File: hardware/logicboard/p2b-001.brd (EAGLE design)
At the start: 91 x 90 mm, 54 parts, among them IC1 74LS06N, IC2 4066N, J1 MKR, J2 GPIO, J3 Vcc, J4 RLY, J5 SPI, J7 DIN5, J8 DIN5, J9 DIN5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

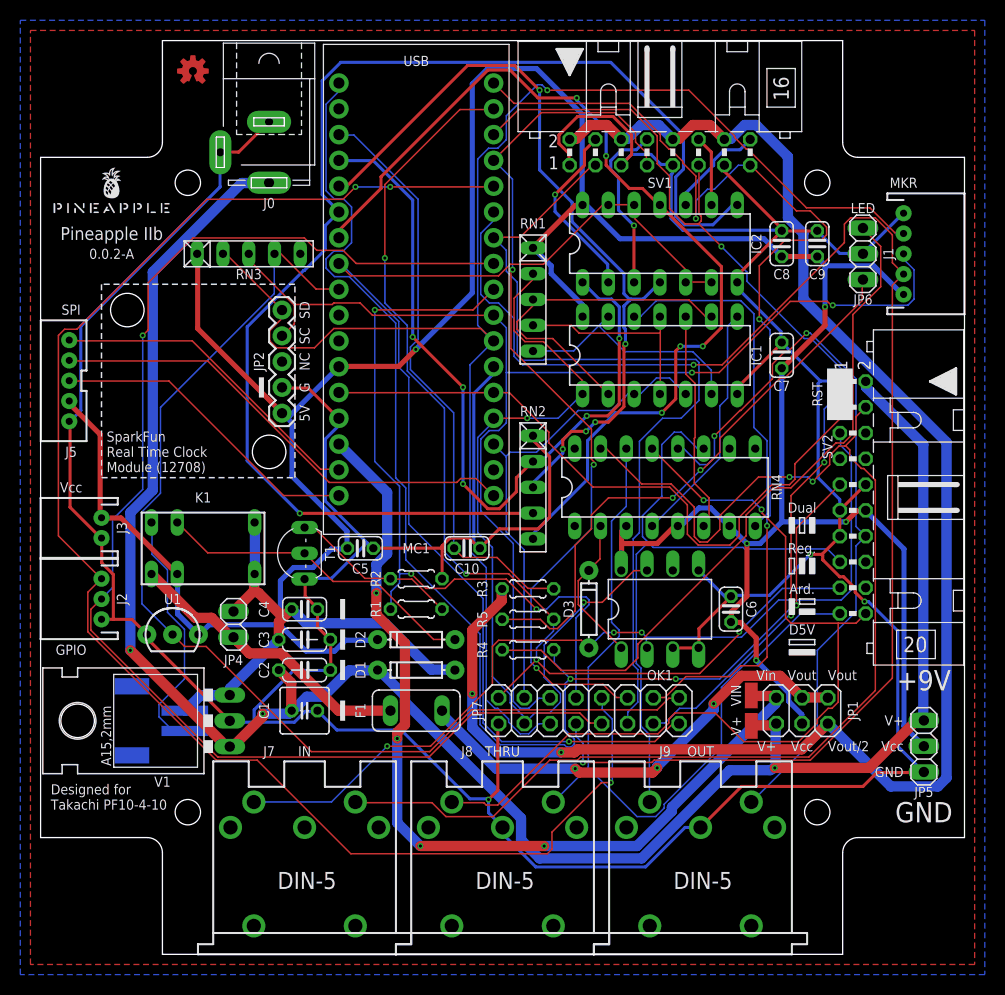
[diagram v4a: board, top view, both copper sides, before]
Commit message: Followed Pineapple II 2.4.0 design. Before autorouting.
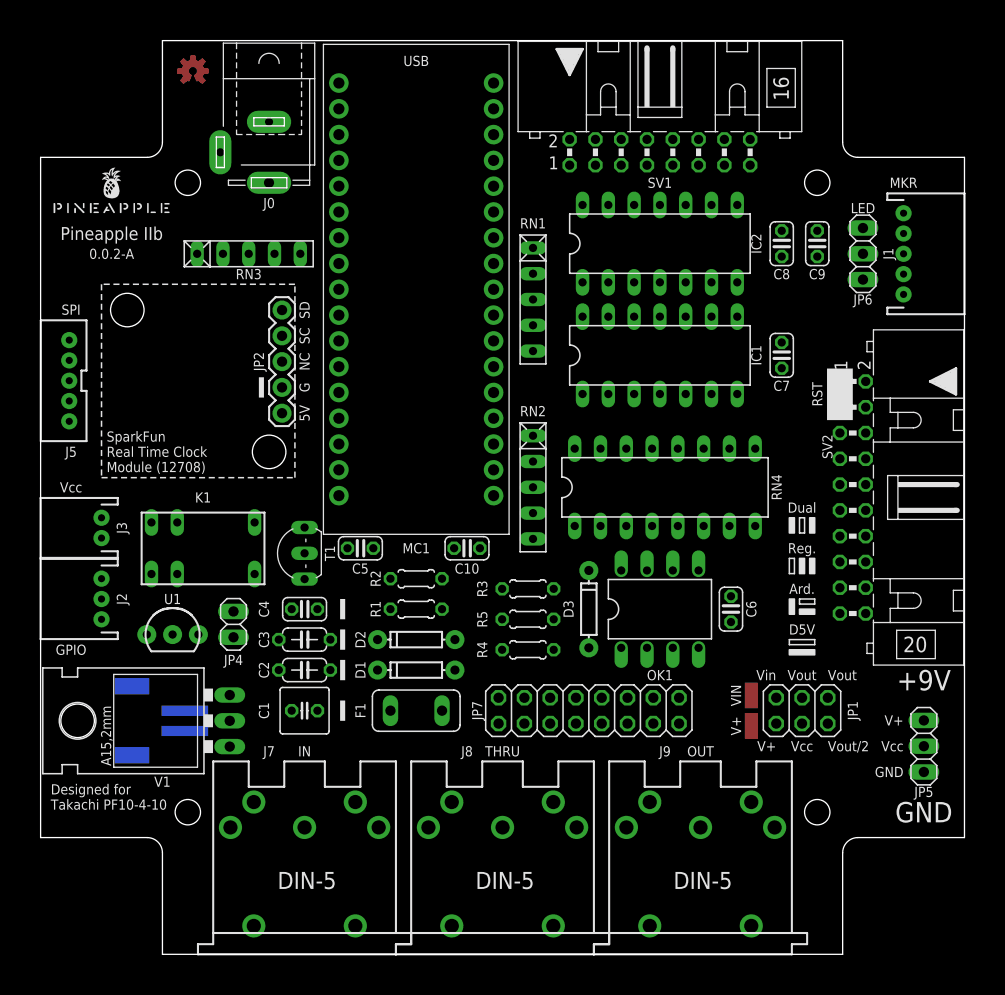
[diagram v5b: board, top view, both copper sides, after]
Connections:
- removed net D7: J1.4, JP7.7, MC1.P$6
- removed net GATE: IC2.12, IC2.13, IC2.5, IC2.6, JP7.15, MC1.P$27
- removed net LED0A: JP6.3, R4.1
- new net D7GATE: IC2.12, IC2.13, IC2.5, IC2.6, J1.4, JP7.7, MC1.P$6
- new net LED2A: JP6.1, R5.1
- new net MNTR: JP7.15, MC1.P$27, OK1.6, RN3.5
- new net MNTRA: OK1.4, RN4.16
- net GND: no longer OK1.4
- net LED1A: now also JP6.3, R4.1; no longer JP6.1, R5.1
- net VCC/2: now also RN4.1
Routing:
- net GND: track 428.7 -> 0.00 mm, vias 3 -> 0
- net VCC: track 321.2 -> 0.00 mm, vias 5 -> 0
- net V+: track 200.8 -> 0.00 mm, vias 3 -> 0
- net VCC/2: track 161.3 -> 0.00 mm, vias 2 -> 0
- net GPIO2: track 153.8 -> 0.00 mm, vias 3 -> 0
- net SDA: track 151.7 -> 0.00 mm, vias 1 -> 0
- net D7: track 144.6 -> 0.00 mm, vias 2 -> 0
- net LED1: track 133.9 -> 0.00 mm, vias 3 -> 0
- net GPIO1: track 131.2 -> 0.00 mm, vias 1 -> 0
- net ANLG3: track 127.0 -> 0.00 mm, vias 1 -> 0
- net SCL: track 124.9 -> 0.00 mm, vias 2 -> 0
- net MISND: track 122.4 -> 0.00 mm, vias 2 -> 0
- net GATE: track 116.9 -> 0.00 mm, vias 1 -> 0
- net LED2: track 110.1 -> 0.00 mm, vias 4 -> 0
- net THS: track 108.8 -> 0.00 mm
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- removed copper zone on layer 1, net GND
- removed copper zone on layer 16, net GND

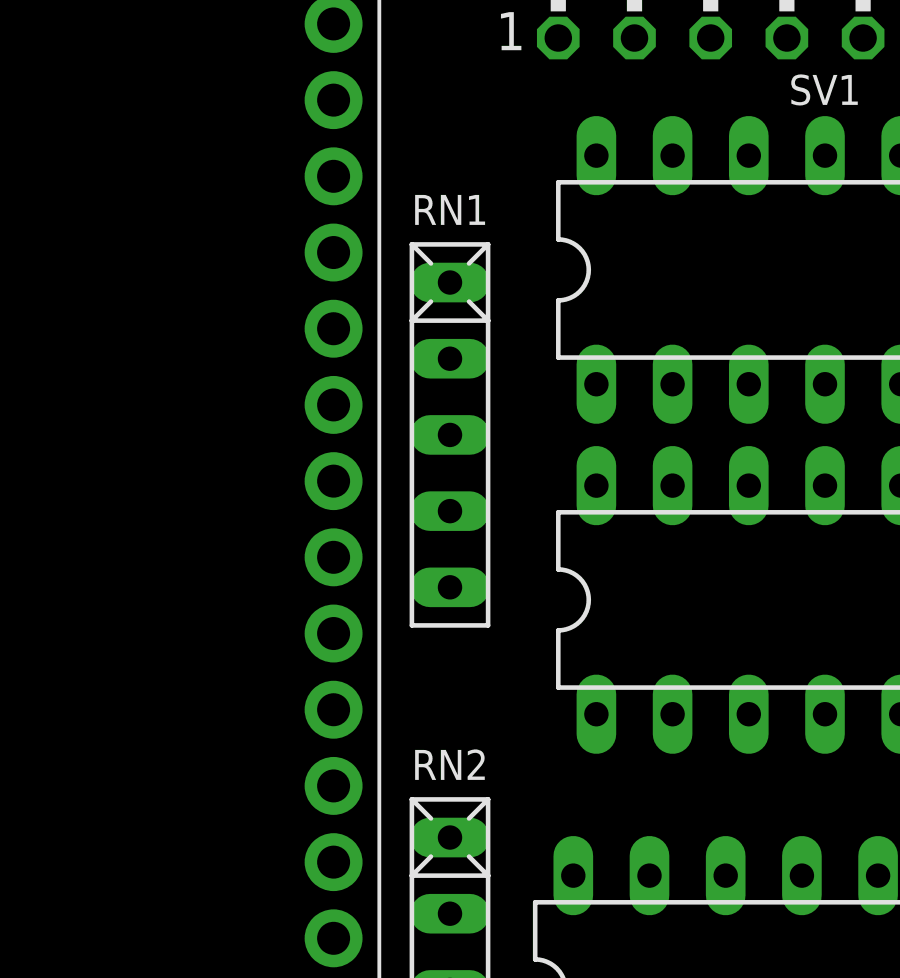
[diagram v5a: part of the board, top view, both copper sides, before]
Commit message: Swapped RN1 and RN2.
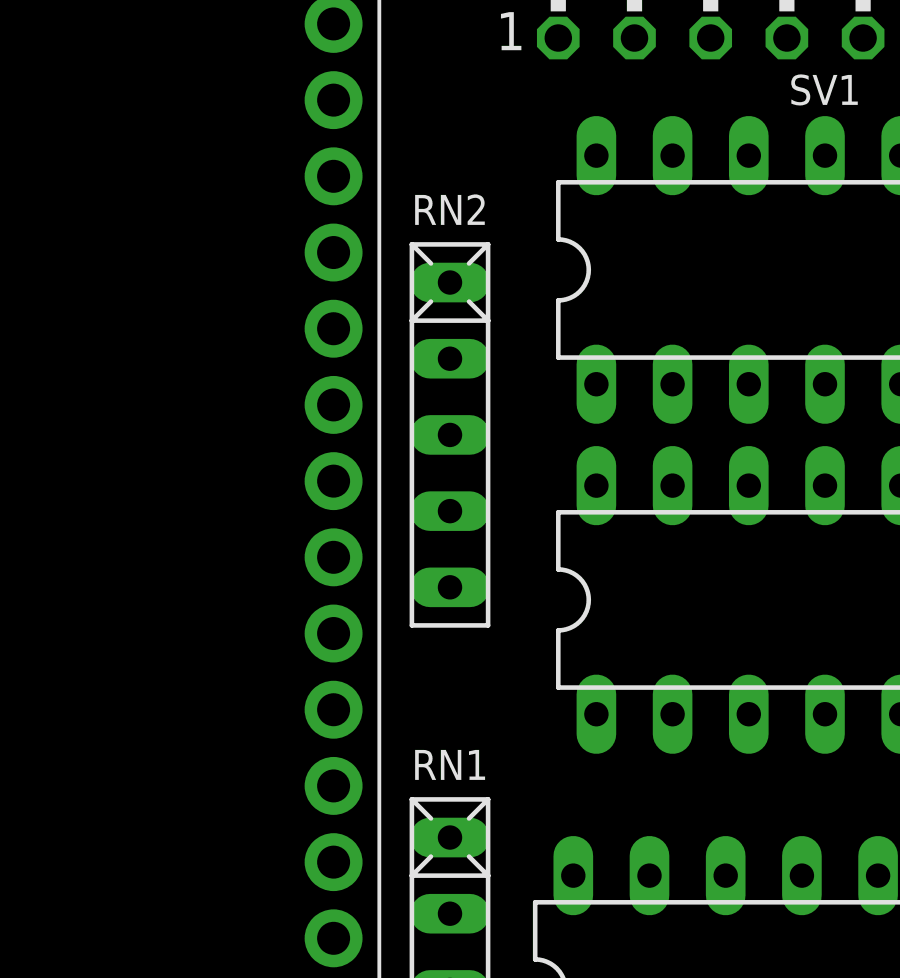
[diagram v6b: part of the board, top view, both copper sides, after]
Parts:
- RN1: value 4.7k -> 10k
- RN2: value 10k -> 4.7k
- moved RN1 18.5 mm to (48.5, 46.0)
- moved RN2 18.5 mm to (48.5, 64.5)
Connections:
- net ANLG1: now also RN1.2; no longer RN2.2
- net ANLG2: now also RN1.3; no longer RN2.3
- net ANLG3: now also RN1.4; no longer RN2.4
- net ANLG4: now also RN1.5; no longer RN2.5
- net GND: now also RN1.1; no longer RN2.1
- net NMO2RTN: now also RN2.5; no longer RN1.5
- net NMORTN: now also RN2.4; no longer RN1.4
- net NMTRTN: now also RN2.3; no longer RN1.3
- net RX: now also RN2.2; no longer RN1.2
- net VCC: now also RN2.1; no longer RN1.1
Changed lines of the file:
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@@
 <attribute name="VALUE" x="37" y="39" size="0.8128" layer="27" ratio="10" rot="R180" align="bottom-center"/>
 </element>
-<element name="RN2" library="resistor-net" library_urn="urn:adsk.eagle:library:343" package="RN-5" package3d_urn="urn:adsk.eagle:package:24976/1" value="10k" x="48.5" y="46" smashed="yes" rot="R270">
+<element name="RN1" library="resistor-net" library_urn="urn:adsk.eagle:library:343" package="RN-5" package3d_urn="urn:adsk.eagle:package:24976/1" value="10k" x="48.5" y="46" smashed="yes" rot="R270">
 <attribute name="MF" value="" x="48.5" y="46" size="1.778" layer="27" rot="R270" display="off"/>
 <attribute name="MPN" value="" x="48.5" y="46" size="1.778" layer="27" rot="R270" display="off"/>
@@
 <attribute name="VALUE" x="40.222" y="37.333" size="1.27" layer="27" ratio="10"/>
 </element>
-<element name="RN1" library="resistor-net" library_urn="urn:adsk.eagle:library:343" package="RN-5" package3d_urn="urn:adsk.eagle:package:24976/1" value="4.7k" x="48.5" y="64.5" smashed="yes" rot="R270">
+<element name="RN2" library="resistor-net" library_urn="urn:adsk.eagle:library:343" package="RN-5" package3d_urn="urn:adsk.eagle:package:24976/1" value="4.7k" x="48.5" y="64.5" smashed="yes" rot="R270">
 <attribute name="MF" value="" x="48.5" y="64.5" size="1.778" layer="27" rot="R270" display="off"/>
 <attribute name="MPN" value="" x="48.5" y="64.5" size="1.778" layer="27" rot="R270" display="off"/>
@@
 <contactref element="C2" pad="2"/>
 <contactref element="V1" pad="GND"/>
-<contactref element="RN2" pad="1"/>
+<contactref element="RN1" pad="1"/>
 <contactref element="J3" pad="1"/>
 <contactref element="SV1" pad="1"/>
@@
 <contactref element="K1" pad="2"/>
 <contactref element="D2" pad="C"/>
-<contactref element="RN1" pad="1"/>
+<contactref element="RN2" pad="1"/>
 <contactref element="U1" pad="3"/>
 <contactref element="J1" pad="5"/>
@@
 <contactref element="MC1" pad="P$28"/>
 <contactref element="IC2" pad="11"/>
-<contactref element="RN2" pad="5"/>
+<contactref element="RN1" pad="5"/>
 <wire x1="29.38" y1="70.58" x2="61" y2="73.81" width="0" layer="19" extent="1-1"/>
 <wire x1="48.5" y1="40.92" x2="61" y2="73.81" width="0" layer="19" extent="1-1"/>
@@
 <contactref element="MC1" pad="P$29"/>
 <contactref element="IC2" pad="8"/>
-<contactref element="RN2" pad="4"/>
+<contactref element="RN1" pad="4"/>
 <wire x1="48.5" y1="43.46" x2="68.62" y2="73.81" width="0" layer="19" extent="1-1"/>
 <wire x1="29.38" y1="73.12" x2="48.5" y2="43.46" width="0" layer="19" extent="1-1"/>
@@
 <contactref element="MC1" pad="P$30"/>
 <contactref element="IC2" pad="4"/>
-<contactref element="RN2" pad="3"/>
+<contactref element="RN1" pad="3"/>
 <wire x1="48.5" y1="46" x2="61" y2="66.19" width="0" layer="19" extent="1-1"/>
 <wire x1="29.38" y1="75.66" x2="61" y2="66.19" width="0" layer="19" extent="1-1"/>
@@
 <contactref element="MC1" pad="P$31"/>
 <contactref element="IC2" pad="1"/>
-<contactref element="RN2" pad="2"/>
+<contactref element="RN1" pad="2"/>
 <wire x1="48.5" y1="48.54" x2="53.38" y2="66.19" width="0" layer="19" extent="1-1"/>
 <wire x1="29.38" y1="78.2" x2="53.38" y2="66.19" width="0" layer="19" extent="1-1"/>
@@
 <signal name="RX">
 <contactref element="MC1" pad="P$14"/>
-<contactref element="RN1" pad="2"/>
+<contactref element="RN2" pad="2"/>
 <contactref element="OK1" pad="7"/>
 <contactref element="IC1" pad="1"/>
@@
 <contactref element="IC1" pad="2"/>
 <contactref element="IC1" pad="9"/>
-<contactref element="RN1" pad="3"/>
+<contactref element="RN2" pad="3"/>
 <wire x1="55.92" y1="55.19" x2="66.08" y2="62.81" width="0" layer="19" extent="1-1"/>
 <wire x1="48.5" y1="64.5" x2="55.92" y2="55.19" width="0" layer="19" extent="1-1"/>
@@
 <contactref element="IC1" pad="4"/>
 <contactref element="IC1" pad="11"/>
-<contactref element="RN1" pad="4"/>
+<contactref element="RN2" pad="4"/>
 <wire x1="61" y1="55.19" x2="61" y2="62.81" width="0" layer="19" extent="1-1"/>
 <wire x1="48.5" y1="61.96" x2="61" y2="62.81" width="0" layer="19" extent="1-1"/>
@@
 <contactref element="IC1" pad="6"/>
 <contactref element="IC1" pad="13"/>
-<contactref element="RN1" pad="5"/>
+<contactref element="RN2" pad="5"/>
 <wire x1="55.92" y1="62.81" x2="66.08" y2="55.19" width="0" layer="19" extent="1-1"/>
 <wire x1="48.5" y1="59.42" x2="55.92" y2="62.81" width="0" layer="19" extent="1-1"/>

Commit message: The new test pad.
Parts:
- removed JP7: (no value), pinhead:2X08
- added SV3: (no value), con-ml:ML14
- moved RN4 1.00 mm to (61.5, 47.0)
- moved C6 0.50 mm to (68.0, 34.5)
- moved C7 0.50 mm to (73.0, 59.5)
- moved C8 0.50 mm to (73.0, 70.5)
- moved C9 0.50 mm to (76.5, 70.5)
- moved D3 0.50 mm to (54.0, 34.5)
- moved IC1 0.50 mm to (61.0, 59.5)
- moved IC2 0.50 mm to (61.0, 70.5)
- moved OK1 0.50 mm to (61.0, 34.5)
- moved R3 0.50 mm to (48.0, 36.5)
- moved R4 0.50 mm to (48.0, 30.5)
- moved R5 0.50 mm to (48.0, 33.5)
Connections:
- net D7GATE: now also SV3.7; no longer JP7.7
- net DTCT1: now also SV3.11; no longer JP7.11
- net DTCT2: now also SV3.12; no longer JP7.12
- net DTCT3: now also SV3.13; no longer JP7.13
- net DTCT4: now also SV3.14; no longer JP7.14
- net GND: now also SV3.1; no longer JP7.1
- net GPIO1: now also SV3.9; no longer JP7.9
- net GPIO2: now also SV3.10; no longer JP7.10
- net LED2: no longer JP7.2
- net MNTR: no longer JP7.15
- net RLY: no longer JP7.8
- net RX: now also SV3.3; no longer JP7.3
- net SCL: now also SV3.6; no longer JP7.6
- net SDA: now also SV3.5; no longer JP7.5
- net THS: now also SV3.8; no longer JP7.16
- net TX: now also SV3.4; no longer JP7.4
- net VCC: now also SV3.2
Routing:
- net GND: track 0.00 -> 405.0 mm, vias 0 -> 3
- net VCC: track 0.00 -> 333.6 mm
- net V+: track 0.00 -> 202.9 mm, vias 0 -> 5
- net LED2: track 0.00 -> 170.4 mm
- net SDA: track 0.00 -> 162.7 mm, vias 0 -> 4
- net SCL: track 0.00 -> 162.3 mm, vias 0 -> 3
- net GPIO2: track 0.00 -> 156.6 mm, vias 0 -> 1
- net VCC/2: track 0.00 -> 151.9 mm, vias 0 -> 9
- net DTCT3: track 0.00 -> 141.5 mm, vias 0 -> 2
- net VIN: track 0.00 -> 137.0 mm, vias 0 -> 4
- net GPIO1: track 0.00 -> 135.1 mm, vias 0 -> 2
- net DTCT2: track 0.00 -> 128.9 mm, vias 0 -> 2
- net ANLG3: track 0.00 -> 127.3 mm, vias 0 -> 5
- net D7GATE: track 0.00 -> 118.7 mm, vias 0 -> 5
- net ANLG2: track 0.00 -> 114.8 mm, vias 0 -> 4
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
